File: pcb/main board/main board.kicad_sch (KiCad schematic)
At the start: 36 parts, among them J10 12V Battery, J11 BAU, J12 Servo 4 Conn, J13 Servo 1 Conn, J14 Servo 2 Conn, J15 Servo 3 Conn, J16 Servo 5 Conn, J17 Servo 6 Conn, J18 Servo 7 Conn, J19 Servo 8 Conn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

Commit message: Almost finished PCB !
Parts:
- A1, A2: footprint Module:RaspberryPi_Pico_Common_Unspecified -> Module:RaspberryPi_Pico_Common_THT
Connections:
- net Motor 1 Activation Pin: now also A1.12 (GPIO9); no longer A1.1 (GPIO0)
- net Motor 2 Activation Pin: now also A1.11 (GPIO8); no longer A1.2 (GPIO1)
- net Motor 3 Activation Pin: now also A1.15 (GPIO11); no longer A1.4 (GPIO2)
- net Motor 4 Activation Pin: now also A1.14 (GPIO10); no longer A1.5 (GPIO3)
- net Servo 1 PWM: now also A1.1 (GPIO0); no longer A1.6 (GPIO4)
- net Servo 2 PWM: now also A1.2 (GPIO1); no longer A1.7 (GPIO5)
- net Servo 3 PWM: now also A1.4 (GPIO2); no longer A1.9 (GPIO6)
- net Servo 4 PWM: now also A1.5 (GPIO3); no longer A1.10 (GPIO7)
- net Servo 5 PWM: now also A1.6 (GPIO4); no longer A1.11 (GPIO8)
- net Servo 6 PWM: now also A1.7 (GPIO5); no longer A1.12 (GPIO9)
- net Servo 7 PWM: now also A1.9 (GPIO6); no longer A1.14 (GPIO10)
- net Servo 8 PWM: now also A1.10 (GPIO7); no longer A1.15 (GPIO11)

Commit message: Added Aisler DRC and corrected errors.
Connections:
- net +5VL: now also A1.39 (VSYS), A2.39 (VSYS); no longer A1.40 (VBUS), A2.40 (VBUS)
- net GNDPWR: now also A1.33 (AGND)
- no-connect marks 0 -> 49

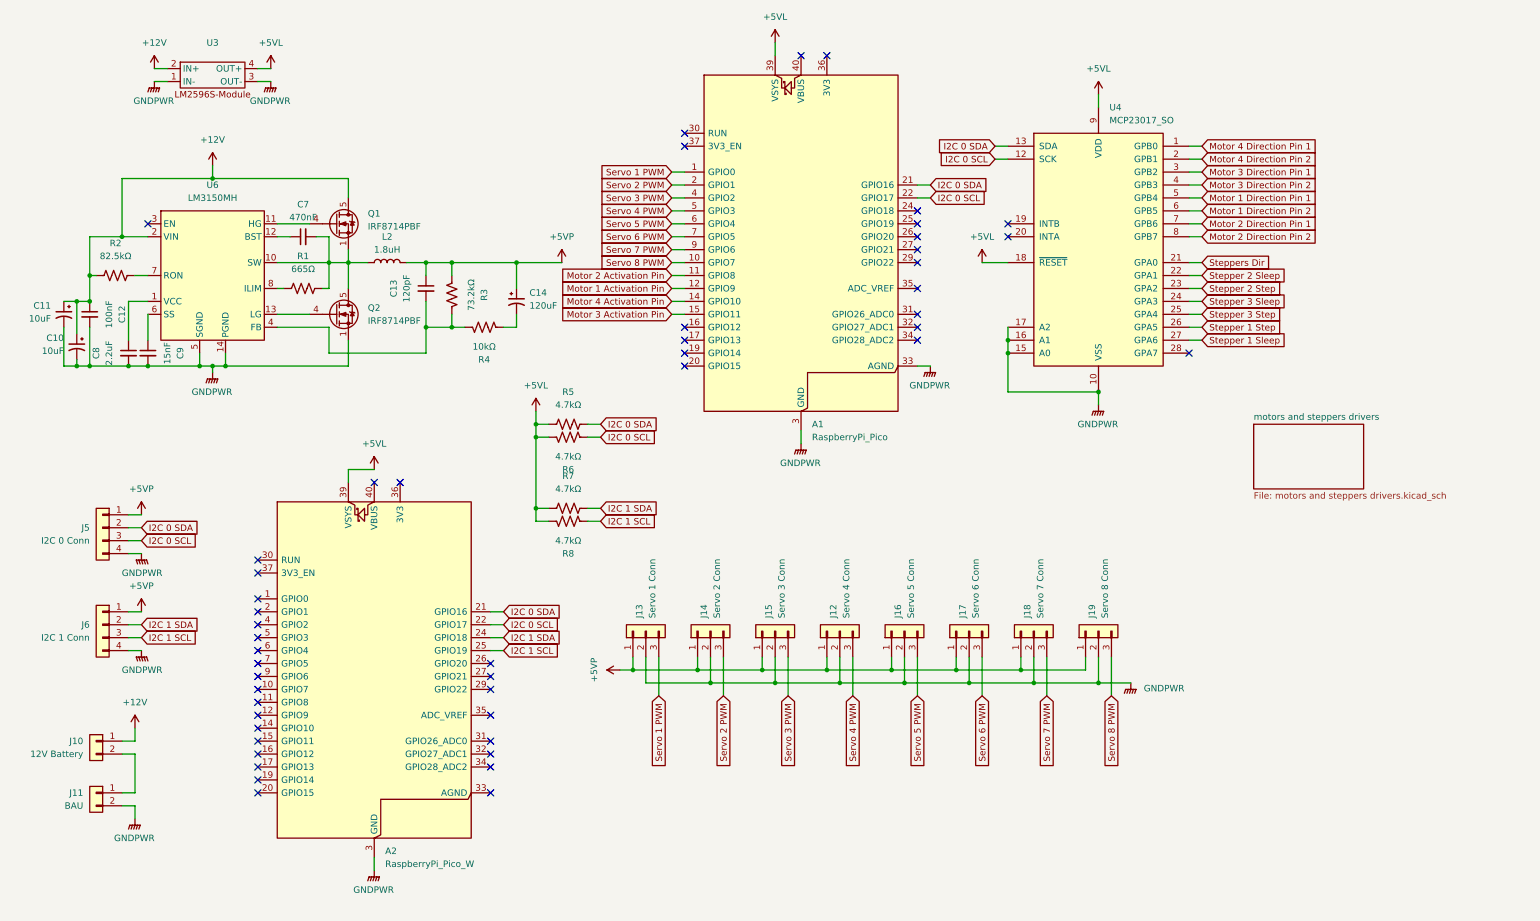
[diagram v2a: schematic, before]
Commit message: Added motors encoders connectors
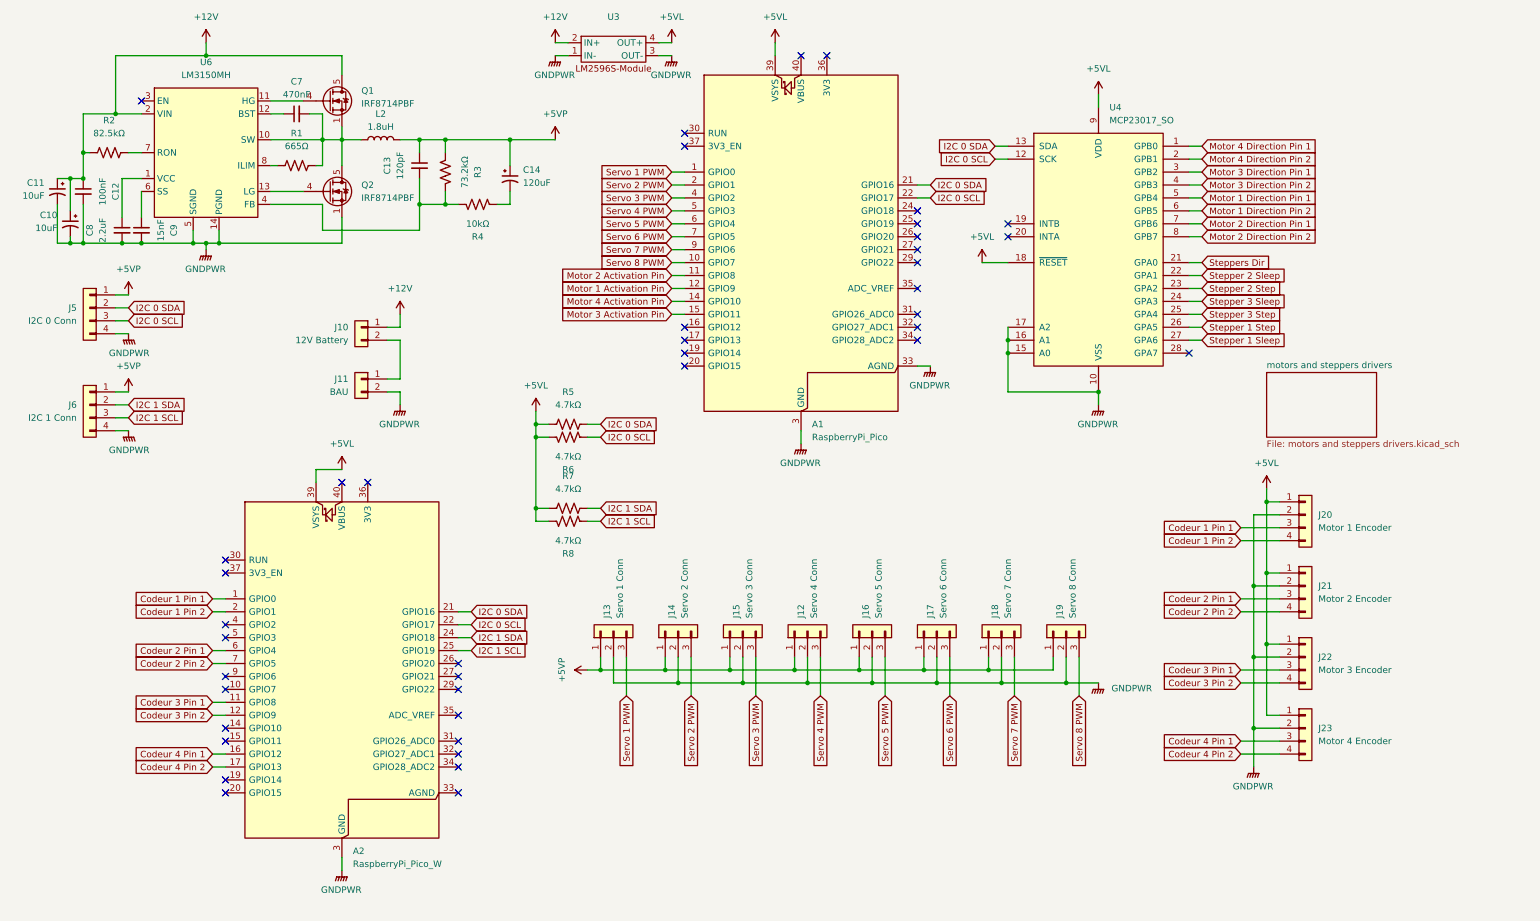
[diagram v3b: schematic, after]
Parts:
- added J20: Motor 1 Encoder, Connector_PinHeader_2.54mm:PinHeader_1x04_P2.54mm_Vertical, symbol Connector_Generic:Conn_01x04
- added J21: Motor 2 Encoder, Connector_PinHeader_2.54mm:PinHeader_1x04_P2.54mm_Vertical, symbol Connector_Generic:Conn_01x04
- added J22: Motor 3 Encoder, Connector_PinHeader_2.54mm:PinHeader_1x04_P2.54mm_Vertical, symbol Connector_Generic:Conn_01x04
- added J23: Motor 4 Encoder, Connector_PinHeader_2.54mm:PinHeader_1x04_P2.54mm_Vertical, symbol Connector_Generic:Conn_01x04
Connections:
- net +5VL: now also J20.1 (Pin_1), J21.1 (Pin_1), J22.1 (Pin_1), J23.1 (Pin_1)
- net GNDPWR: now also J20.2 (Pin_2), J21.2 (Pin_2), J22.2 (Pin_2), J23.2 (Pin_2)
- net Codeur 1 Pin 1: now reaches A2.1 (GPIO0)
- net Codeur 1 Pin 1: now also J20.3 (Pin_3)
- net Codeur 3 Pin 1: now reaches A2.11 (GPIO8)
- net Codeur 3 Pin 1: now also J22.3 (Pin_3)
- net Codeur 3 Pin 2: now reaches A2.12 (GPIO9)
- net Codeur 3 Pin 2: now also J22.4 (Pin_4)
- net Codeur 4 Pin 1: now reaches A2.16 (GPIO12)
- net Codeur 4 Pin 1: now also J23.3 (Pin_3)
- net Codeur 4 Pin 2: now reaches A2.17 (GPIO13)
- net Codeur 4 Pin 2: now also J23.4 (Pin_4)
- net Codeur 1 Pin 2: now reaches A2.2 (GPIO1)
- net Codeur 1 Pin 2: now also J20.4 (Pin_4)
- net Codeur 2 Pin 1: now reaches A2.6 (GPIO4)
- net Codeur 2 Pin 1: now also J21.3 (Pin_3)
- net Codeur 2 Pin 2: now reaches A2.7 (GPIO5)
- net Codeur 2 Pin 2: now also J21.4 (Pin_4)
- no-connect marks 49 -> 41
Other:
- moved on the sheet: A2, C10, C11, C12, C13, C14, C7, C8, C9, J10, J11, J12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

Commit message: Changed empreinte and rewired them to match commanded ones
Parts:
- C10, C11: footprint Capacitor_THT:CP_Radial_D5.0mm_P2.50mm -> Capacitor_THT:CP_Radial_D6.3mm_P2.50mm
- C12, C9: footprint Capacitor_THT:C_Disc_D4.3mm_W1.9mm_P5.00mm -> Capacitor_THT:C_Disc_D3.8mm_W2.6mm_P2.50mm
- C8: footprint Capacitor_THT:C_Disc_D4.3mm_W1.9mm_P5.00mm -> Capacitor_THT:C_Radial_D6.3mm_H5.0mm_P2.50mm
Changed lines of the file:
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@@
 			)
 		)
-		(property "Footprint" "Capacitor_THT:CP_Radial_D5.0mm_P2.50mm"
+		(property "Footprint" "Capacitor_THT:CP_Radial_D6.3mm_P2.50mm"
 			(at 20.32 49.53 0)
 			(effects
@@
 			)
 		)
-		(property "Footprint" "Capacitor_THT:CP_Radial_D5.0mm_P2.50mm"
+		(property "Footprint" "Capacitor_THT:CP_Radial_D6.3mm_P2.50mm"
 			(at 22.86 55.88 0)
 			(effects
@@
 			)
 		)
-		(property "Footprint" "Capacitor_THT:C_Disc_D4.3mm_W1.9mm_P5.00mm"
+		(property "Footprint" "Capacitor_THT:C_Disc_D3.8mm_W2.6mm_P2.50mm"
 			(at 36.83 57.15 0)
 			(effects
@@
 			)
 		)
-		(property "Footprint" "Capacitor_THT:C_Disc_D4.3mm_W1.9mm_P5.00mm"
+		(property "Footprint" "Capacitor_THT:C_Radial_D6.3mm_H5.0mm_P2.50mm"
 			(at 33.02 57.15 0)
 			(effects
@@
 			)
 		)
-		(property "Footprint" "Capacitor_THT:C_Disc_D4.3mm_W1.9mm_P5.00mm"
+		(property "Footprint" "Capacitor_THT:C_Disc_D3.8mm_W2.6mm_P2.50mm"
 			(at 25.4 49.53 0)
 			(effects

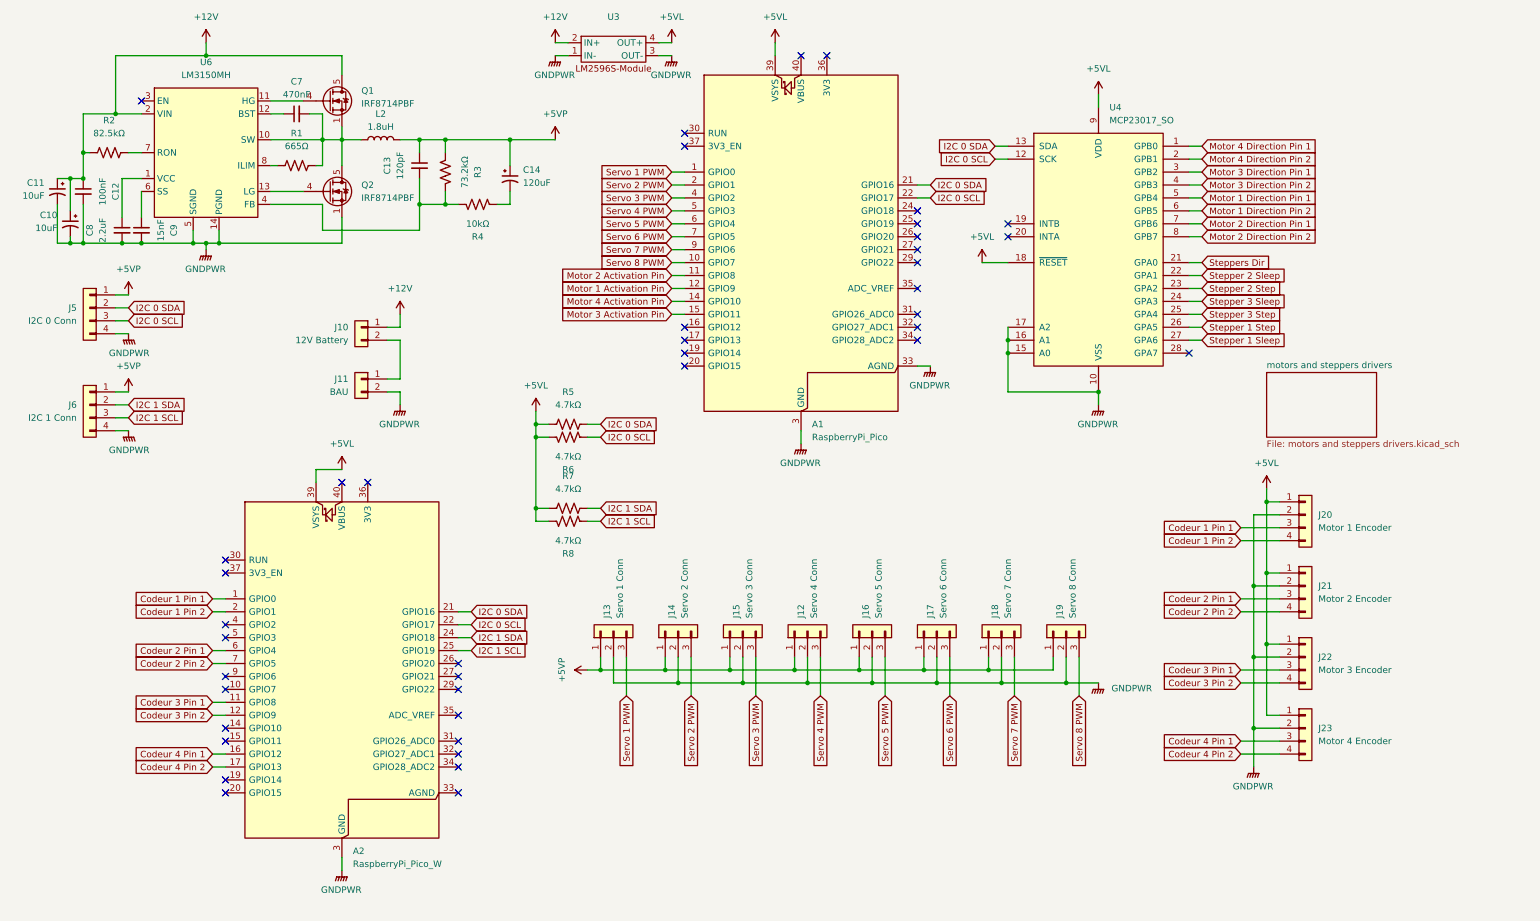
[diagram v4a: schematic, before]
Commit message: Finished correcting and updating footprints for capacitors and started to change connectors footprints
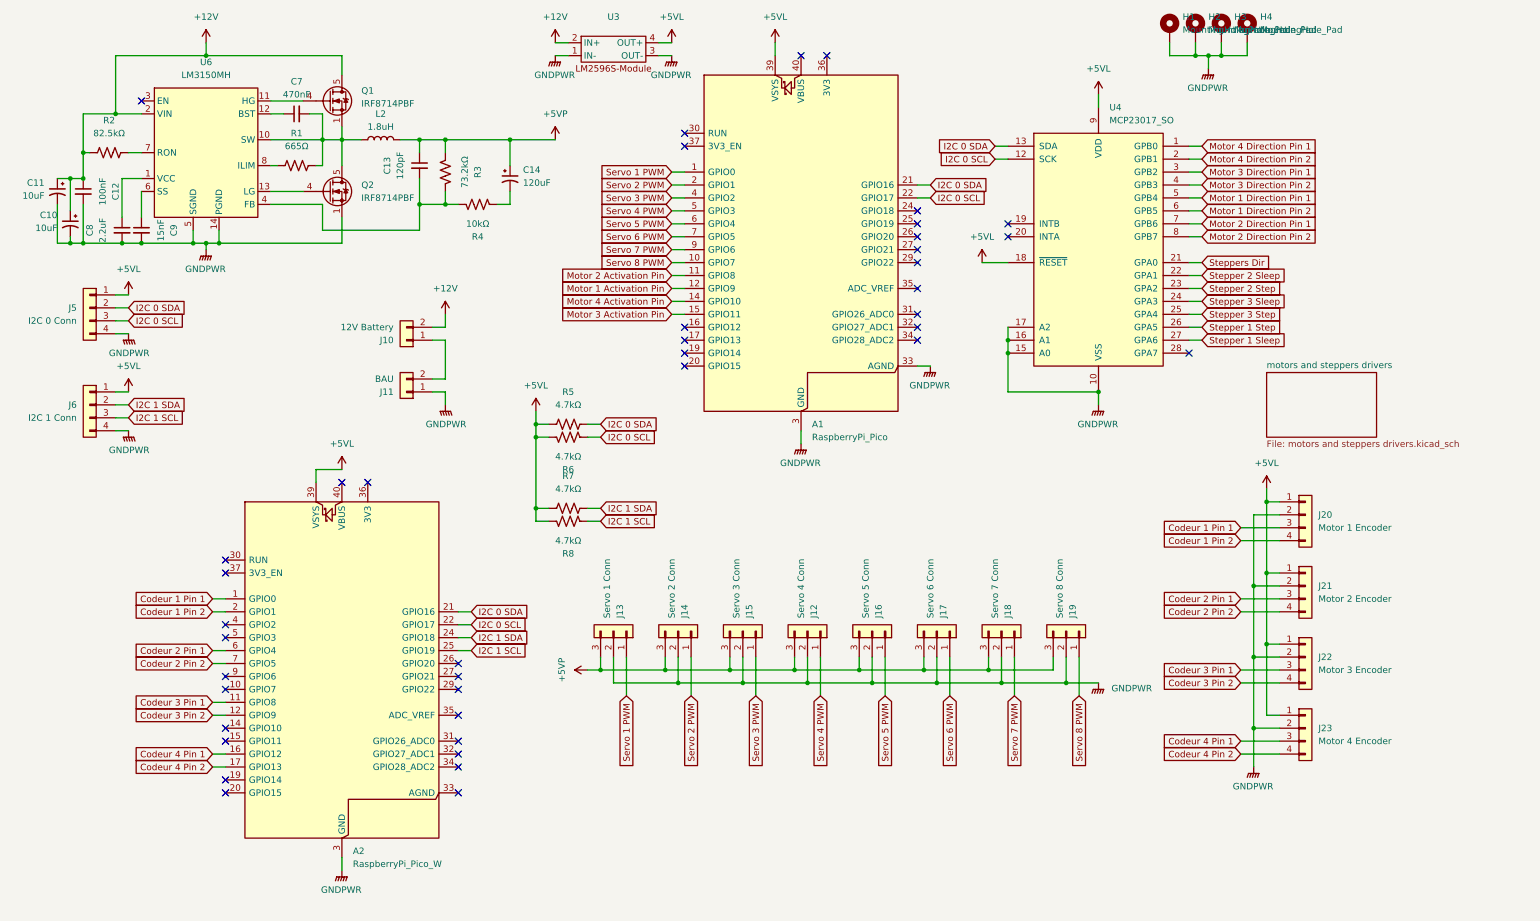
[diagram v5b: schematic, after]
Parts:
- added H1, H2, H3, H4: MountingHole_Pad, MountingHole:MountingHole_3.2mm_M3_Pad, symbol Mechanical:MountingHole_Pad
- J10, J11: footprint Connector_PinHeader_2.54mm:PinHeader_1x02_P2.54mm_Vertical -> Connector_Molex:Molex_KK-254_AE-6410-02A_1x02_P2.54mm_Vertical
- J12, J13, J14, J15, J16, J17, J18, J19: footprint Connector_PinHeader_2.54mm:PinHeader_1x03_P2.54mm_Vertical -> Connector_Molex:Molex_KK-254_AE-6410-03A_1x03_P2.54mm_Vertical
- J20, J21, J22, J23, J5, J6: footprint Connector_PinHeader_2.54mm:PinHeader_1x04_P2.54mm_Vertical -> Connector_Molex:Molex_KK-254_AE-6410-04A_1x04_P2.54mm_Vertical
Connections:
- net +12V: now also J10.2 (Pin_2); no longer J10.1 (Pin_1)
- net +5VL: now also J5.1 (Pin_1), J6.1 (Pin_1)
- net +5VP: now also J12.3 (Pin_3), J13.3 (Pin_3), J14.3 (Pin_3), J15.3 (Pin_3), J16.3 (Pin_3), J17.3 (Pin_3), J18.3 (Pin_3), J19.3 (Pin_3); no longer J12.1 (Pin_1), J13.1 (Pin_1), J14.1 (Pin_1), J15.1 (Pin_1), J16.1 (Pin_1), J17.1 (Pin_1), J18.1 (Pin_1), J19.1 (Pin_1), J5.1 (Pin_1), J6.1 (Pin_1)
- net GNDPWR: now also J11.1 (Pin_1), H1.1, H2.1, H3.1, H4.1; no longer J11.2 (Pin_2)
- net Servo 1 PWM: now also J13.1 (Pin_1); no longer J13.3 (Pin_3)
- net Servo 2 PWM: now also J14.1 (Pin_1); no longer J14.3 (Pin_3)
- net Servo 3 PWM: now also J15.1 (Pin_1); no longer J15.3 (Pin_3)
- net Servo 4 PWM: now also J12.1 (Pin_1); no longer J12.3 (Pin_3)
- net Servo 5 PWM: now also J16.1 (Pin_1); no longer J16.3 (Pin_3)
- net Servo 6 PWM: now also J17.1 (Pin_1); no longer J17.3 (Pin_3)
- net Servo 7 PWM: now also J18.1 (Pin_1); no longer J18.3 (Pin_3)
- net Servo 8 PWM: now also J19.1 (Pin_1); no longer J19.3 (Pin_3)
- new net: J10.1 (Pin_1), J11.2 (Pin_2)
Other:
- moved on the sheet: J10, J11, J12, J13, J14, J15, J16, J17, J18, J19
